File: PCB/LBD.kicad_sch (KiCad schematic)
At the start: 39 parts, among them Q1 AO3400A, Q2 AO3400A, U1 RP2040-ZERO

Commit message: bruh
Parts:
- removed C1, C2: 470u, Capacitor_SMD:CP_Elec_8x10.5, symbol Device:C_Polarized_US
- removed D1, D10, D11, D12, D13, D14, D15, D16, D17, D18, D19, D2, D20, D21, D22, D23, D24, D3, D4, D5, D6, D7, D8, D9: IN-S126ESGHIR, IN_S126ESGHIR:LED_IN-S126ESGHIR, symbol IN-S126ESGHIR:IN-S126ESGHIR
- removed Q1, Q2: AO3400A, Package_TO_SOT_SMD:SOT-23, symbol Transistor_FET:AO3400A
- removed R1, R2, R3, R4, R6, R7, R8, R9: 6.2, Resistor_SMD:R_1206_3216Metric, symbol Device:R_US
- removed R10, R5: 10K, Resistor_SMD:R_0805_2012Metric, symbol Device:R_US
- removed U1: RP2040-ZERO, RP2040-ZERO:MODULE_RP2040-ONE, symbol RP2040-ZERO:RP2040-ZERO
- added J1: USB4155-03-C_REVA, USB4155-03-C_REVA:GCT_USB4155-03-C_REVA, symbol LBD_Library:USB4155-03-C_REVA
- added U1: (no value), symbol LBD_Library:RP2040-Tiny

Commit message: worked on schematic
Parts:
- removed U1: (no value), symbol LBD_Library:RP2040-Tiny
- added C1: 22uF, symbol Device:C_Small
- added C2: 4.7uF, symbol Device:C_Small
- added R1, R2: 5.1k, symbol Device:R_US
- added R3: 100k, symbol Device:R_US
- added U1: RP2040, Package_DFN_QFN:QFN-56-1EP_7x7mm_P0.4mm_EP3.2x3.2mm, symbol MCU_RaspberryPi:RP2040
- added U2: TPSM828214SILR, SIL0010D-MFG, symbol LBD_Library:TPSM828214SILR
- added U3: AT25SF128A-SHB-T, IC8_AT25SF128A-SHB-T_ADO, symbol LBD_Library:AT25SF128A-SHB-T
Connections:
- net GND: now reaches J1.A1 (GND_A)
- net GND: now also J1.A12 (GND_A__1), J1.B1 (GND_B), J1.B12 (GND_B__1), J1.S1 (SHELL_GND), J1.S2 (SHELL_GND__1), C1.2, C2.2, R1.2, R2.1, U2.10 (GND), U2.9 (GND)
- net VBUS: now reaches J1.A4 (VBUS_A)
- net VBUS: now also J1.A9 (VBUS_A__1), J1.B4 (VBUS_B), J1.B9 (VBUS_B__1), C2.1, U2.1 (VIN), U2.2 (VIN), U2.3 (EN)
- net at J1.A5 (CC1): now also R2.2
- net DP: now reaches J1.A6 (DP1)
- net DP: now also J1.B6 (DP2)
- net DN: now reaches J1.A7 (DN1)
- net DN: now also J1.B7 (DN2)
- net at J1.B5 (CC2): now also R1.1
- new net: U1.1 (IOVDD), U1.10 (IOVDD), U1.22 (IOVDD), U1.33 (IOVDD), U1.42 (IOVDD), U1.49 (IOVDD)
- new net: U1.23 (DVDD), U1.50 (DVDD)
- new net +3.3V: C1.1, R3.2, U2.5 (VOUT), U2.6 (VOUT), U2.7 (VOUT), U2.8 (FB)
- new net PG: R3.1, U1.26 (RUN), U2.4 (PG)
- no-connect marks 0 -> 10

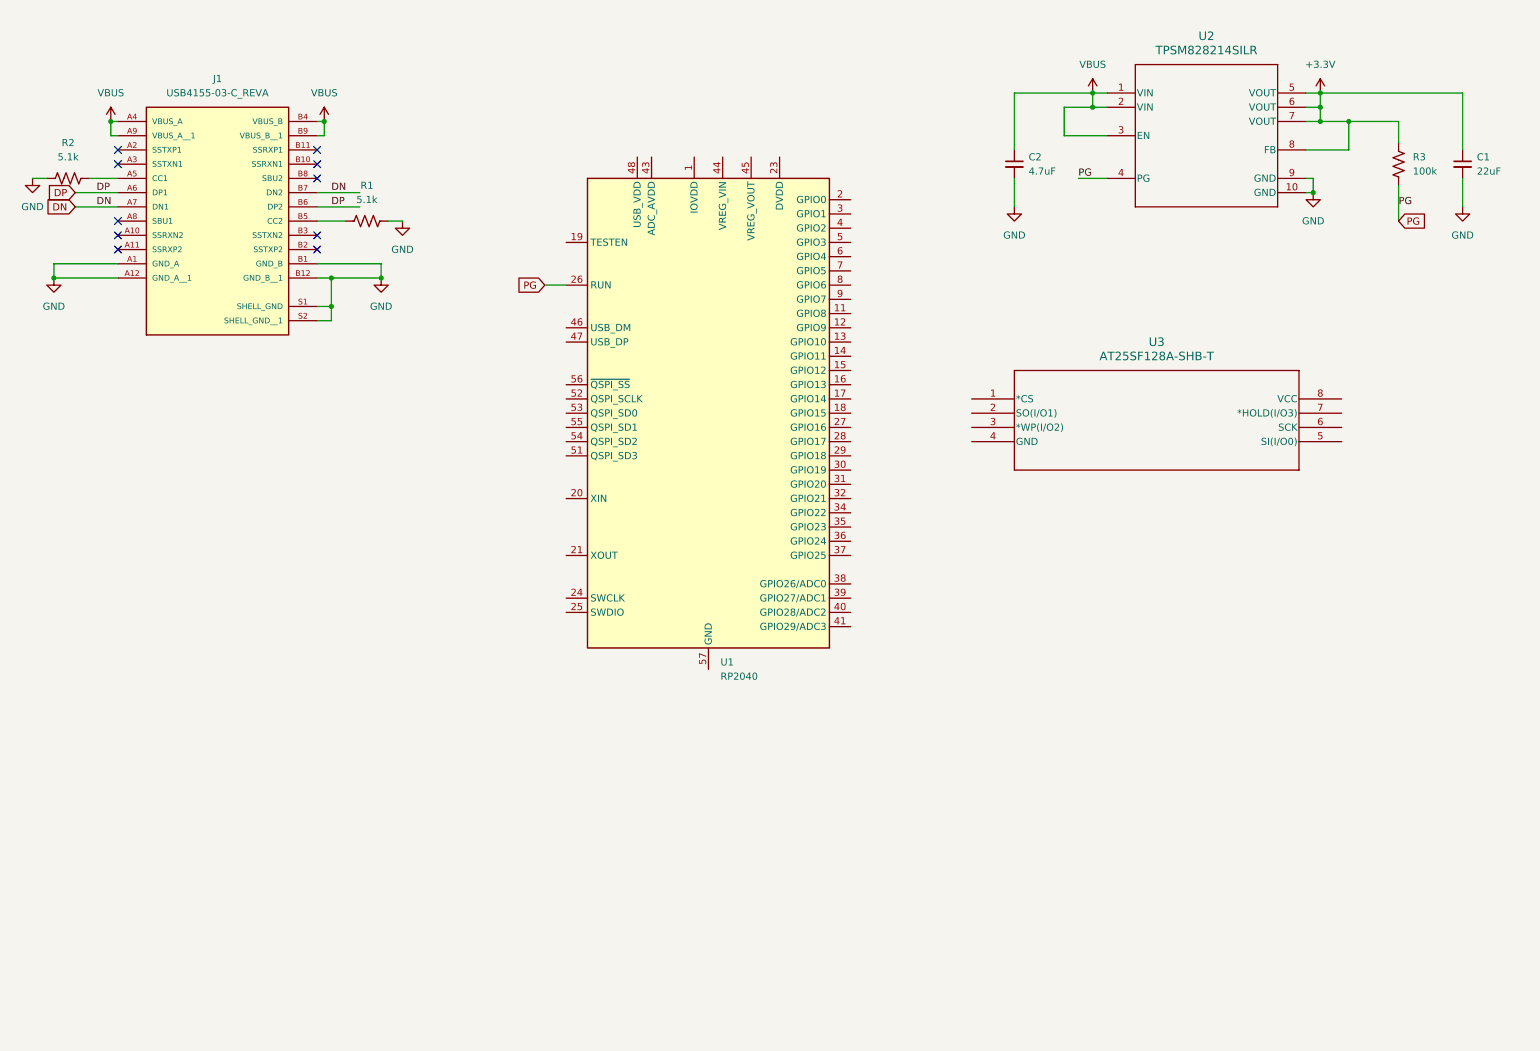
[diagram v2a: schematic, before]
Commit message: finished core, flash, crystal oscillator, and power regulation
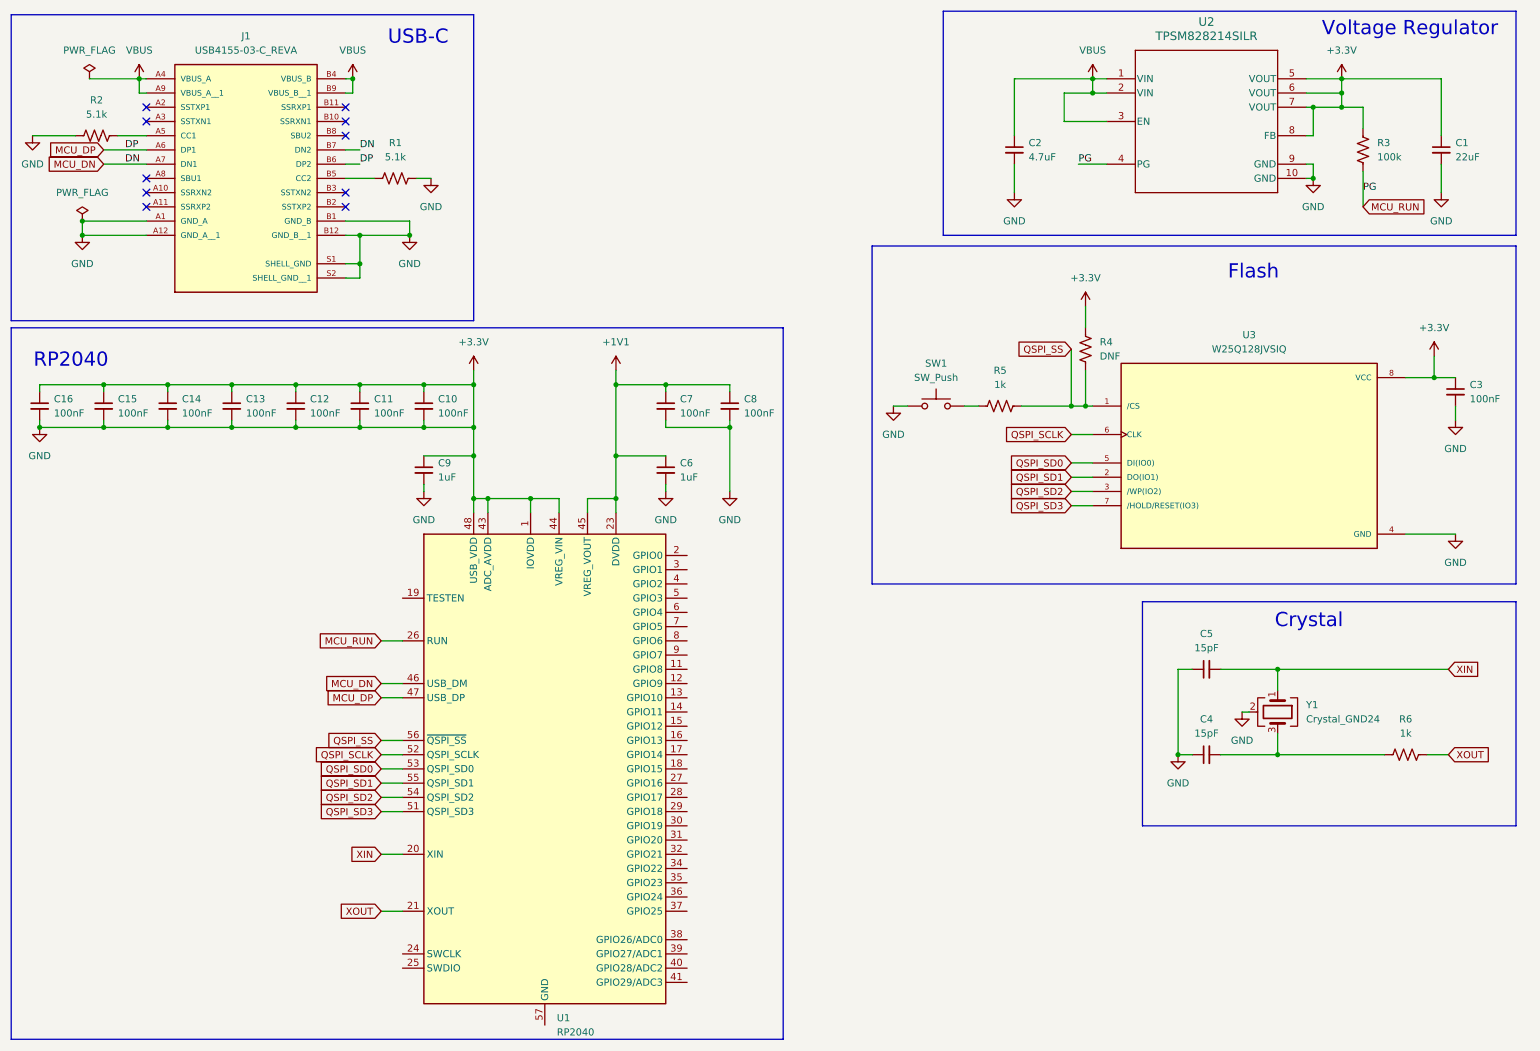
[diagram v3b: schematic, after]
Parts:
- removed U3: AT25SF128A-SHB-T, IC8_AT25SF128A-SHB-T_ADO, symbol LBD_Library:AT25SF128A-SHB-T
- added C10, C11, C12, C13, C14, C15, C16, C3, C7, C8: 100nF, symbol Device:C_Small
- added C4, C5: 15pF, symbol Device:C_Small
- added C6, C9: 1uF, symbol Device:C_Small
- added R4: DNF, symbol Device:R_US
- added R5, R6: 1k, symbol Device:R_US
- added SW1: SW_Push, symbol Switch:SW_Push
- added U3: W25Q128JVSIQ, W25Q128JVSIQ:SOIC127P790X216-8N, symbol LBD_Library:W25Q128JVSIQ
- added Y1: Crystal_GND24, symbol Device:Crystal_GND24
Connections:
- net DN is gone; now on net MCU_DN: J1.A7 (DN1), J1.B7 (DN2)
- net DP is gone; now on net MCU_DP: J1.A6 (DP1), J1.B6 (DP2)
- net GND is gone; now on net +3.3V: C1.2, C2.2, J1.A1 (GND_A), J1.A12 (GND_A__1), J1.B1 (GND_B), J1.B12 (GND_B__1), J1.S1 (SHELL_GND), J1.S2 (SHELL_GND__1), R1.2, R2.1, U2.10 (GND), U2.9 (GND)
- net +3.3V: now also U1.1 (IOVDD), U1.10 (IOVDD), U1.22 (IOVDD), U1.33 (IOVDD), U1.42 (IOVDD), U1.43 (ADC_AVDD), U1.44 (VREG_VIN), U1.48 (USB_VDD), U1.49 (IOVDD), C10.1, C10.2, C11.1, C11.2, C12.1, C12.2, C13.1, C13.2, C14.1, C14.2, C15.1, C15.2, C16.1, C16.2, C3.1, C3.2, C4.1, C5.1, C6.2, C7.2, C8.2, C9.1, C9.2, R4.2, SW1.1, U3.4 (GND), U3.8 (VCC), Y1.2 (G), Y1.4 (G)
- net XIN: now reaches U1.20 (XIN)
- net XIN: now also C5.2, Y1.1
- net XOUT: now reaches U1.21 (XOUT)
- net XOUT: now also R6.1
- net +1V1: now reaches U1.23 (DVDD), U1.50 (DVDD)
- net +1V1: now also U1.45 (VREG_VOUT), C6.1, C7.1, C8.1
- net MCU_DN: now reaches U1.46 (USB_DM)
- net MCU_DP: now reaches U1.47 (USB_DP)
- net QSPI_SD3: now reaches U1.51 (QSPI_SD3)
- net QSPI_SD3: now also U3.7 (/HOLD/RESET(IO3))
- net QSPI_SCLK: now reaches U1.52 (QSPI_SCLK)
- net QSPI_SCLK: now also U3.6 (CLK)
- net QSPI_SD0: now reaches U1.53 (QSPI_SD0)
- net QSPI_SD0: now also U3.5 (DI(IO0))
- net QSPI_SD2: now reaches U1.54 (QSPI_SD2)
- net QSPI_SD2: now also U3.3 (/WP(IO2))
- net QSPI_SD1: now reaches U1.55 (QSPI_SD1)
- net QSPI_SD1: now also U3.2 (DO(IO1))
- net QSPI_SS: now reaches U1.56 (~{QSPI_SS})
- net QSPI_SS: now also R4.1, R5.1, U3.1 (/CS)
- net PG renamed MCU_RUN
- new net: C4.2, R6.2, Y1.3
- new net: R5.2, SW1.2
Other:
- note added: "Crystal"
- note added: "Flash"
- note added: "RP2040"
- note added: "USB-C"
- note added: "Voltage Regulator"
- company: (none) -> Chaos
- title: (none) -> LBD (Lott-Bespitting Diode)
- moved on the sheet: C1, C2, J1, R1, R2, R3, U1, U2
